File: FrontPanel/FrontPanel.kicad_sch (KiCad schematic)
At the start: 73 parts, among them J1 CPU, J2 Backplane, U1 74LS38, U2 74LS38, U3 74LS123, U4 NE555P

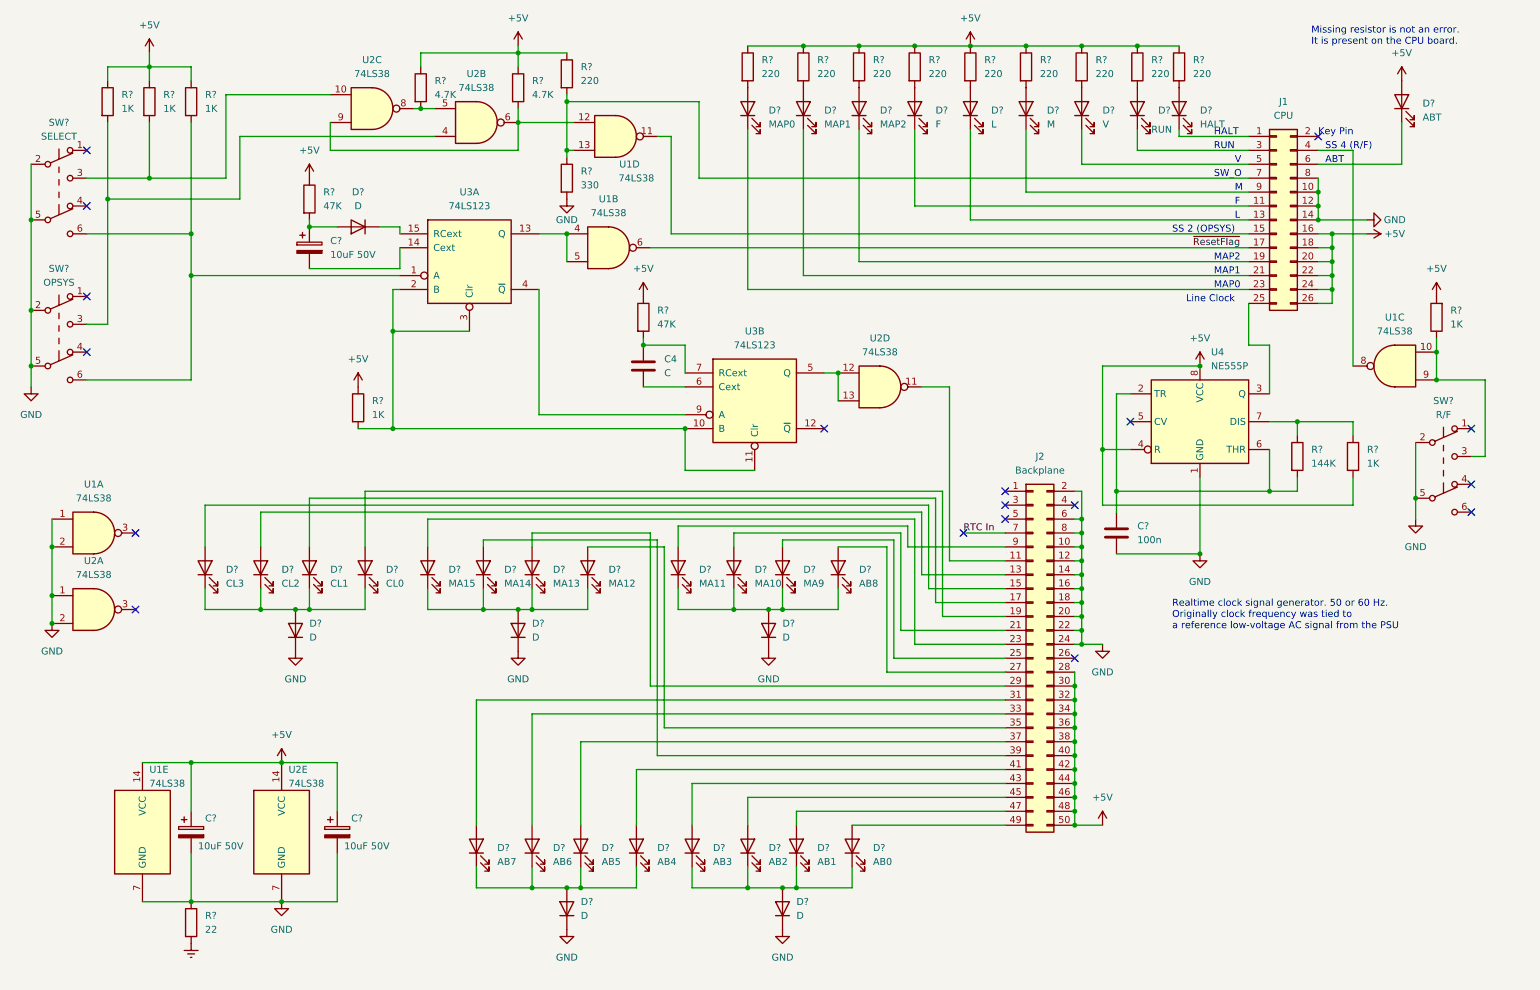
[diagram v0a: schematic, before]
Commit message: Initial PCB
PCB with sizes and critical components placement. No routing yet.
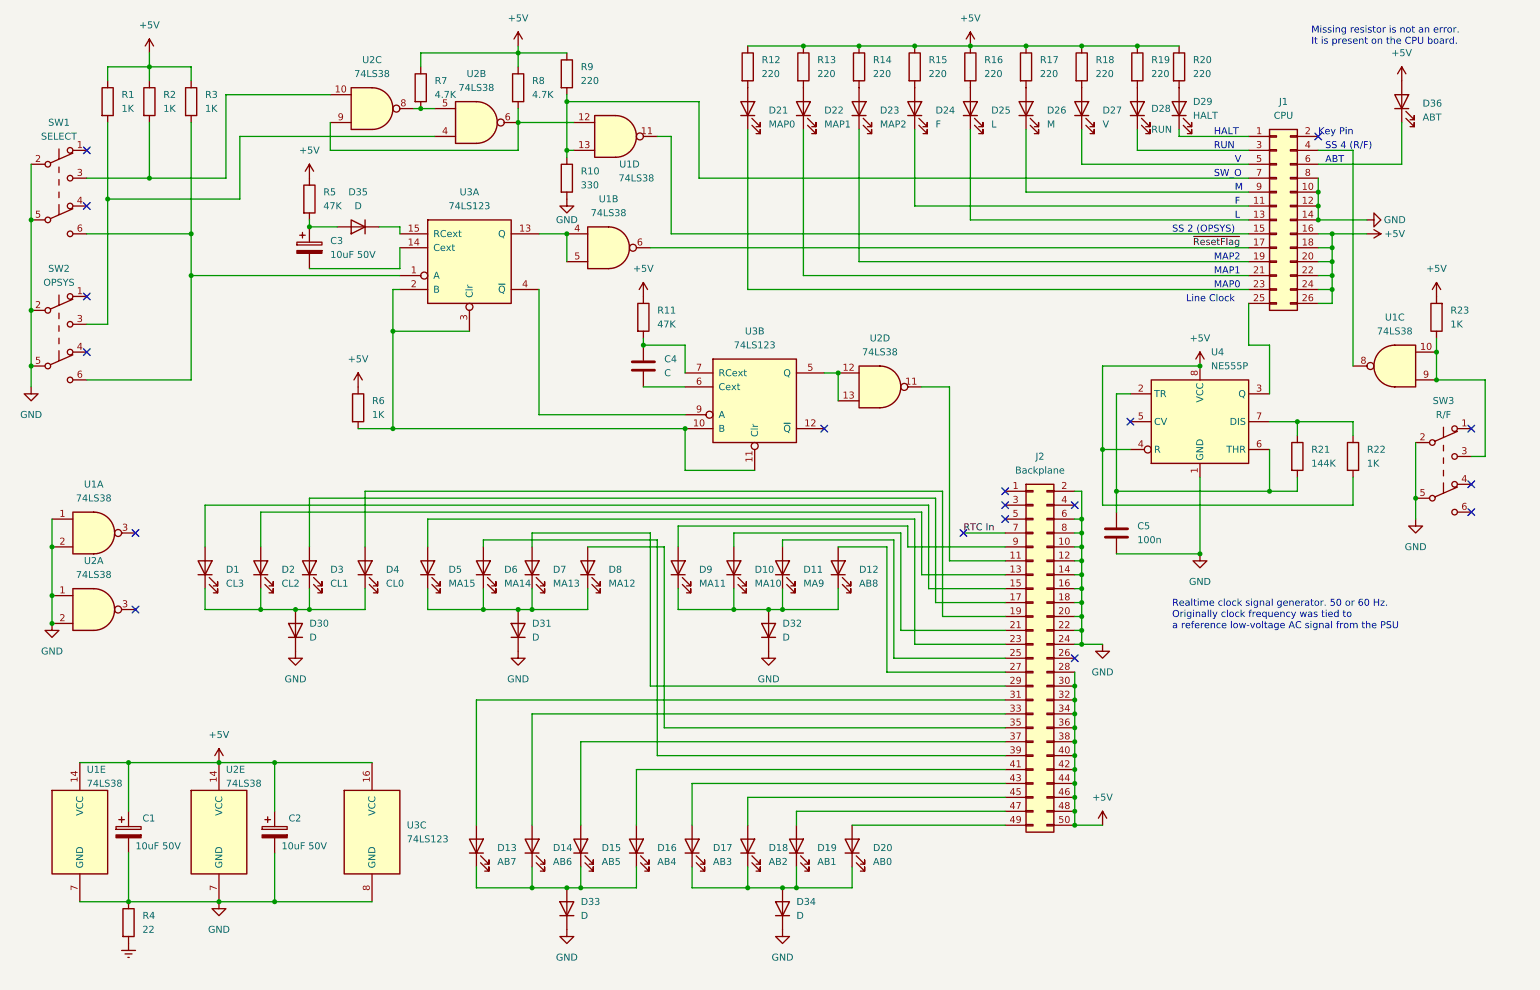
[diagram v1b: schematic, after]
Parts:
- added unit 3 of U3
- C1, C2, C3: renamed from C?; footprint (none) -> Capacitor_THT:CP_Radial_D8.0mm_P3.50mm
- C4: footprint (none) -> Capacitor_THT:C_Disc_D4.3mm_W1.9mm_P5.00mm
- C5: renamed from C?; footprint (none) -> Capacitor_THT:C_Disc_D4.3mm_W1.9mm_P5.00mm
- D1, D10, D11, D12, D13, D14, D15, D16, D17, D18, D19, D2, D20, D21, D22, D23, D24, D25, D26, D27, D28, D29, D3, D36, D4, D5, D6, D7, D8, D9: renamed from D?; footprint (none) -> LED_THT:LED_D5.0mm
- D30, D31, D32, D33, D34, D35: renamed from D?; footprint (none) -> Diode_THT:D_A-405_P7.62mm_Horizontal
- J1: footprint Connector_IDC:IDC-Header_2x13_P2.54mm_Horizontal -> Connector_IDC:IDC-Header_2x13_P2.54mm_Vertical
- J2: footprint (none) -> Connector_IDC:IDC-Header_2x25_P2.54mm_Vertical
- R1, R10, R11, R12, R13, R14, R15, R16, R17, R18, R19, R2, R20, R21, R22, R23, R3, R4, R5, R6, R7, R8, R9: renamed from R?; footprint (none) -> Resistor_THT:R_Axial_DIN0207_L6.3mm_D2.5mm_P10.16mm_Horizontal
- U1, U2: footprint (none) -> Package_DIP:DIP-14_W7.62mm
- U3: footprint (none) -> Package_DIP:DIP-16_W7.62mm
- gave numbers to parts that had none: 3
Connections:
- net +5V: now also U3.16 (VCC)
- net GND: now also U3.8 (GND)
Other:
- moved on the sheet: C1, C2, R4, U1E, U2E

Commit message: FrontPanel: Parts placement
Placed all the parts close to original layout.
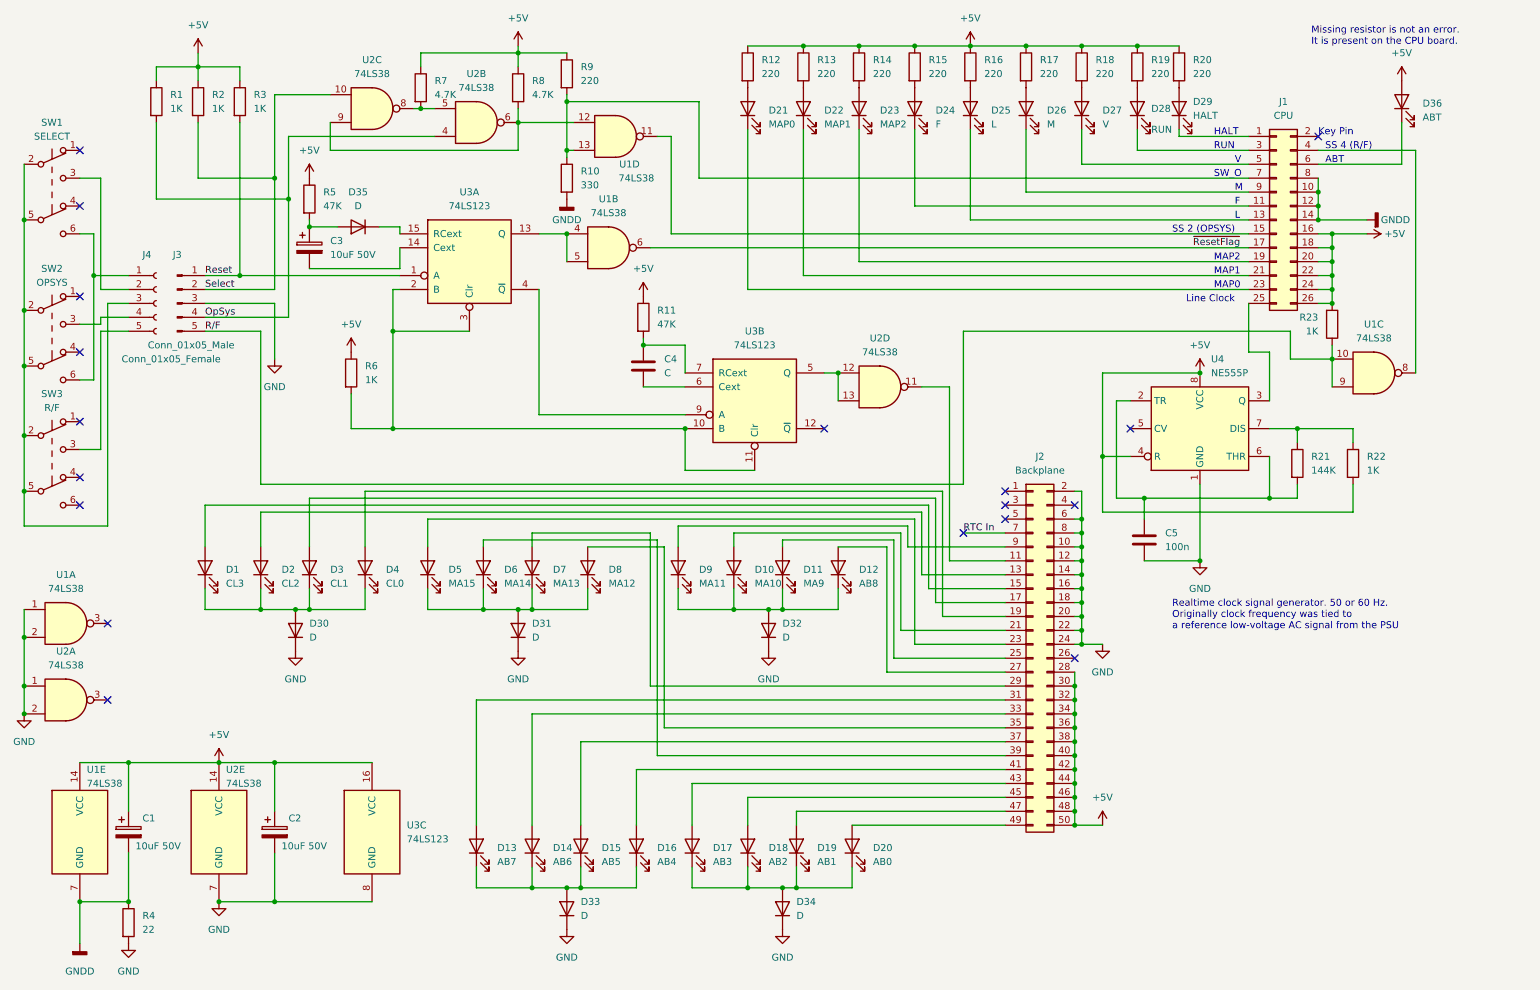
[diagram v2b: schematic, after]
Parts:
- added J3: Conn_01x05_Male, Connector_PinHeader_2.54mm:PinHeader_1x05_P2.54mm_Vertical, symbol Connector:Conn_01x05_Male
- added J4: Conn_01x05_Female, symbol Connector:Conn_01x05_Female
- C1, C2, C3: footprint Capacitor_THT:CP_Radial_D8.0mm_P3.50mm -> Capacitor_THT:CP_Axial_L18.0mm_D6.5mm_P25.00mm_Horizontal
- D30, D31, D32, D33, D34, D35: footprint Diode_THT:D_A-405_P7.62mm_Horizontal -> Diode_THT:D_A-405_P10.16mm_Horizontal
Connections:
- net Earth is gone; now on net GND: R4.2
- net GND: now also J3.3 (Pin_3); no longer C1.2, J1.10 (Pin_10), J1.12 (Pin_12), J1.14 (Pin_14), J1.8 (Pin_8), R10.2, R4.1, SW1.2 (B), SW1.5 (B), SW2.2 (B), SW2.5 (B), SW3.2 (B), SW3.5 (B), U1.7 (GND)
- net OpSys: now reaches R1.2, U2.4
- net OpSys: now also J3.4 (Pin_4); no longer SW2.3 (C)
- net at SW1.6 (C), SW2.6 (C): now also J4.1 (Pin_1); no longer R3.2, U3.1 (A)
- net R/F: now reaches R23.1, U1.10, U1.9
- net R/F: now also J3.5 (Pin_5); no longer SW3.3 (C)
- net Select: now reaches R2.2, U2.10
- net Select: now also J3.2 (Pin_2); no longer SW1.3 (C)
- new net: J4.3 (Pin_3), SW1.2 (B), SW1.5 (B), SW2.2 (B), SW2.5 (B), SW3.2 (B), SW3.5 (B)
- new net: J4.4 (Pin_4), SW2.3 (C)
- new net: J4.2 (Pin_2), SW1.3 (C)
- new net: J4.5 (Pin_5), SW3.3 (C)
- new net GNDD: C1.2, J1.10 (Pin_10), J1.12 (Pin_12), J1.14 (Pin_14), J1.8 (Pin_8), R10.2, R4.1, U1.7 (GND)
- new net Reset: J3.1 (Pin_1), R3.2, U3.1 (A)
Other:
- moved on the sheet: C5, R1, R2, R21, R22, R23, R3, R6, SW1, SW2, SW3, U1A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
